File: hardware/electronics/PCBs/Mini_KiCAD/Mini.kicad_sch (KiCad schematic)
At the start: 0 parts

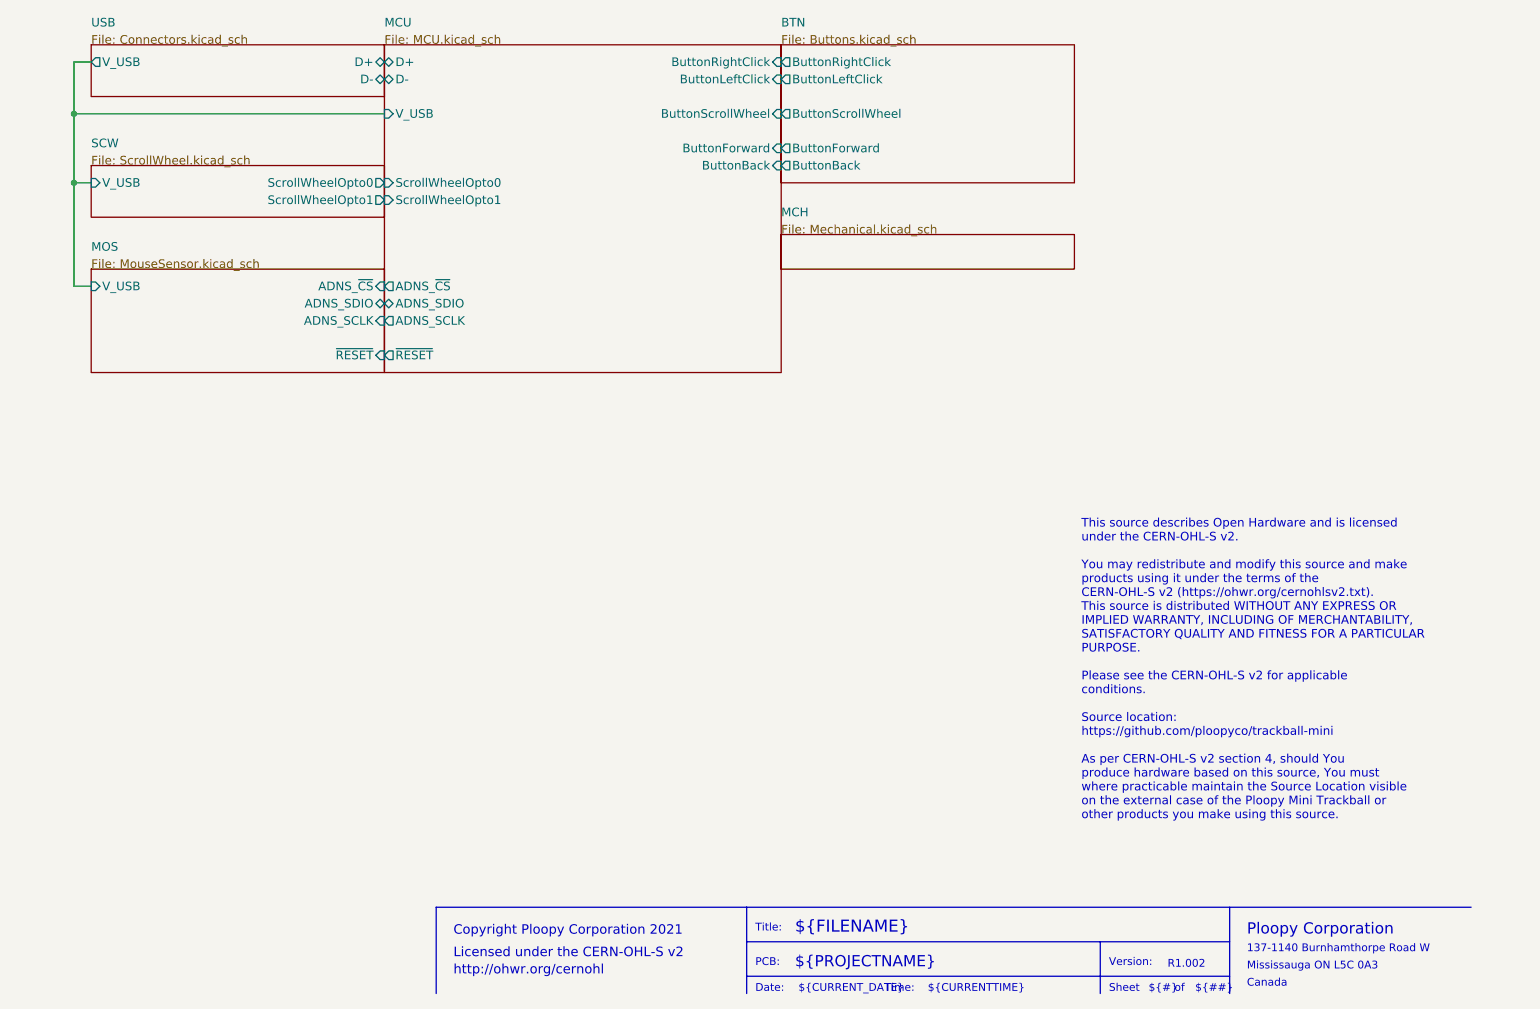
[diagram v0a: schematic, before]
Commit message: Initial commit of the modified Ploopy Mini PCB with RP2040, PMW3360 and mid-mounted USB-C
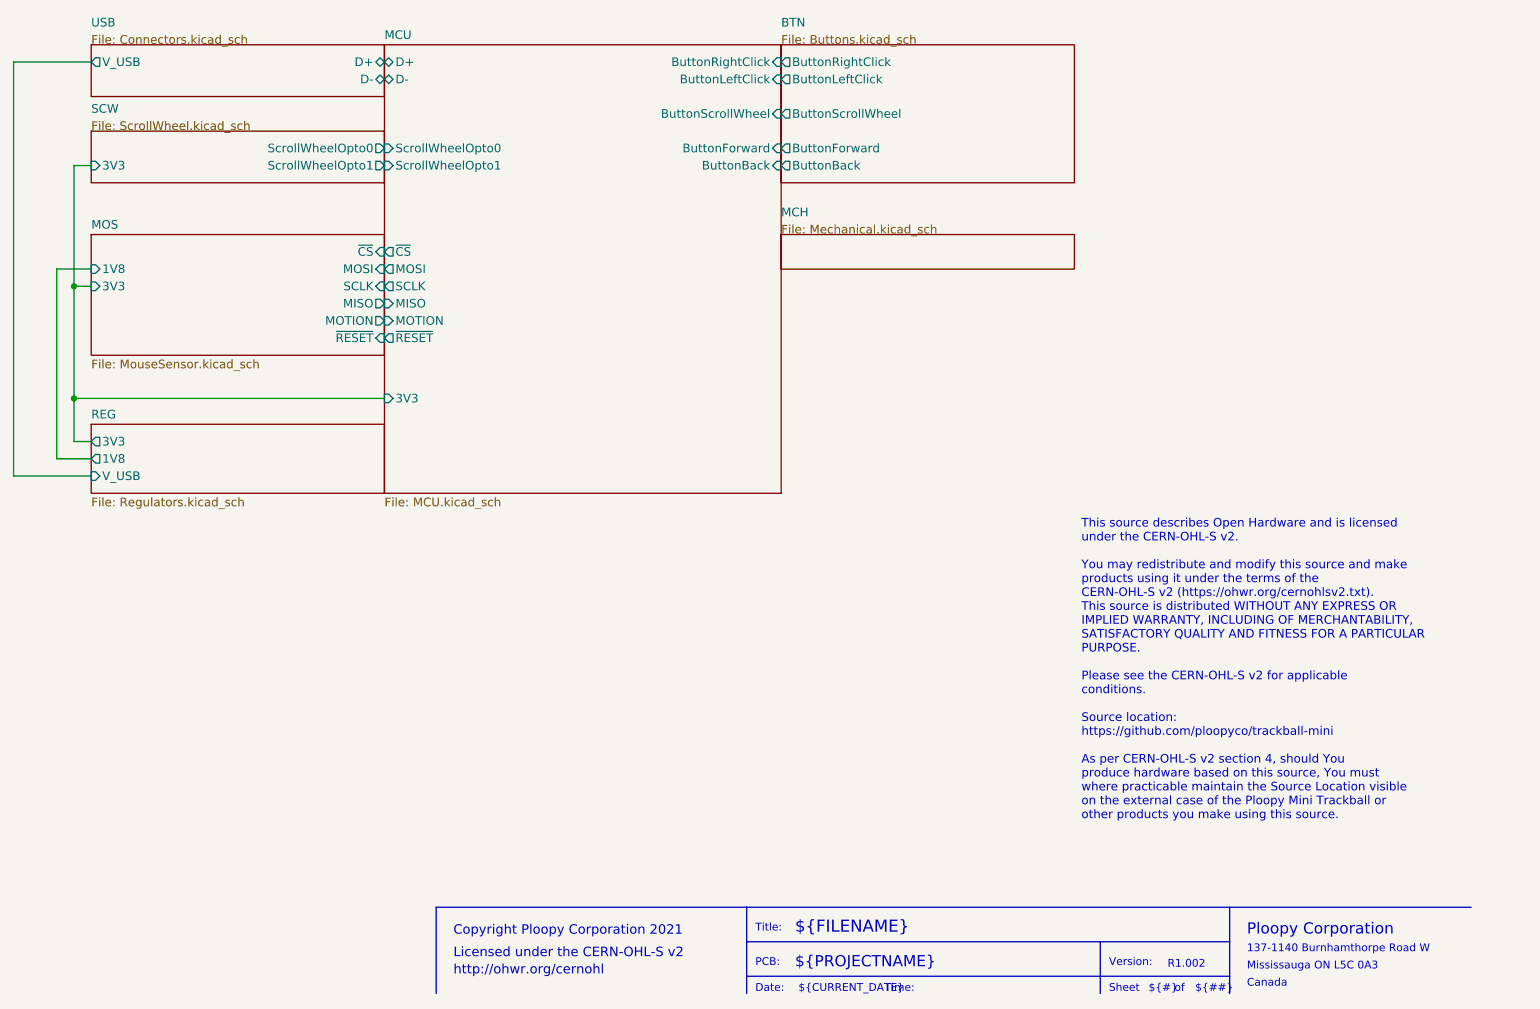
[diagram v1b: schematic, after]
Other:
- added sheet REG (Regulators.kicad_sch)
- sheet MCU ports: added 3V3, MISO, MOSI, MOTION, SCLK, ~{CS}; removed ADNS_SCLK, ADNS_SDIO, ADNS_~{CS}, V_USB
- sheet MOS ports: added 1V8, 3V3, MISO, MOSI, MOTION, SCLK, ~{CS}; removed ADNS_SCLK, ADNS_SDIO, ADNS_~{CS}, V_USB
- sheet SCW ports: added 3V3; removed V_USB
- note removed: "${CURRENTTIME}"
